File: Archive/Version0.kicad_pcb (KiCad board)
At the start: 2 copper layers, 14 parts, among them P1 CONN_BATT, P2 CONN_LOAD, P3 CONN_VREG, P4 CONN_FEATHER12, P5 CONN_FEATHER16, P6 CONN_RB, P7 CONN_WS, P8 CONN_RB, P9 CONN_WS, Q1 Q_NMOS_GDS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

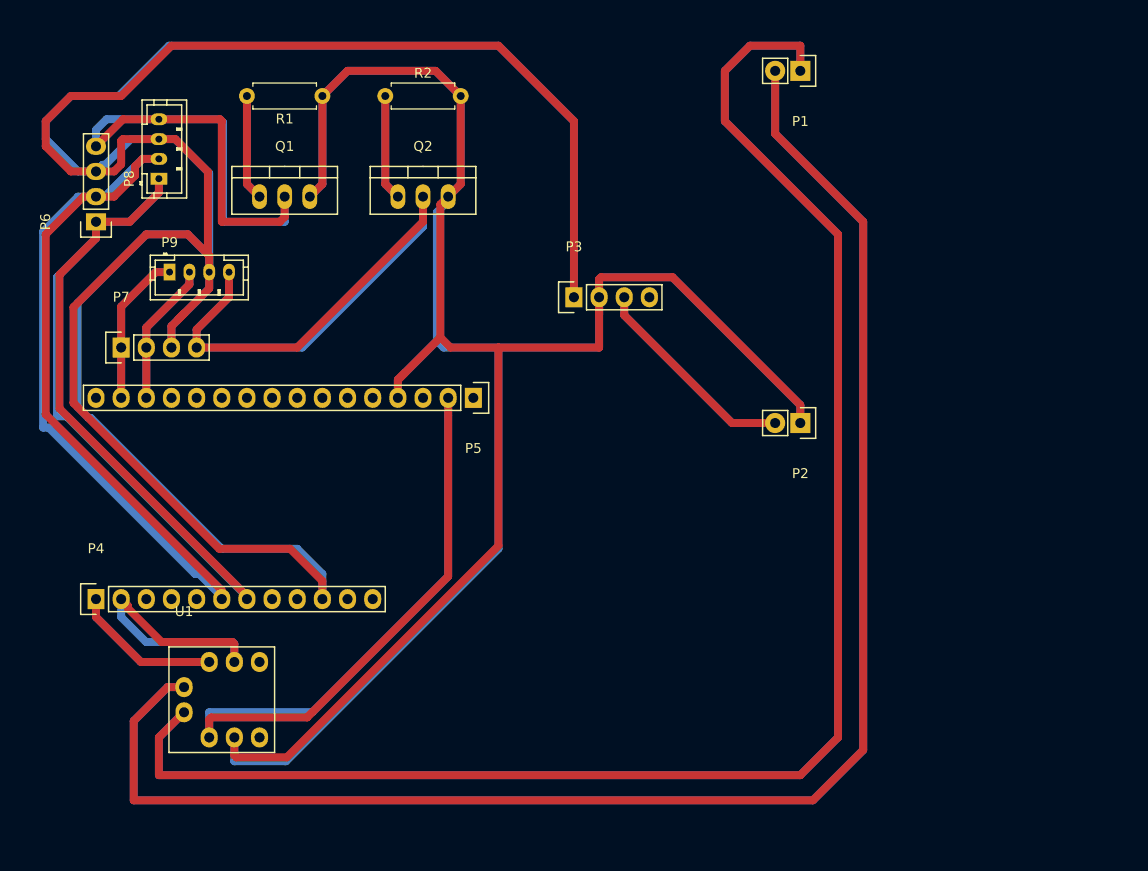
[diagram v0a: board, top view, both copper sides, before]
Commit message: Fixed Gerbers
Updated the footprint pins on the Fuel Gauge
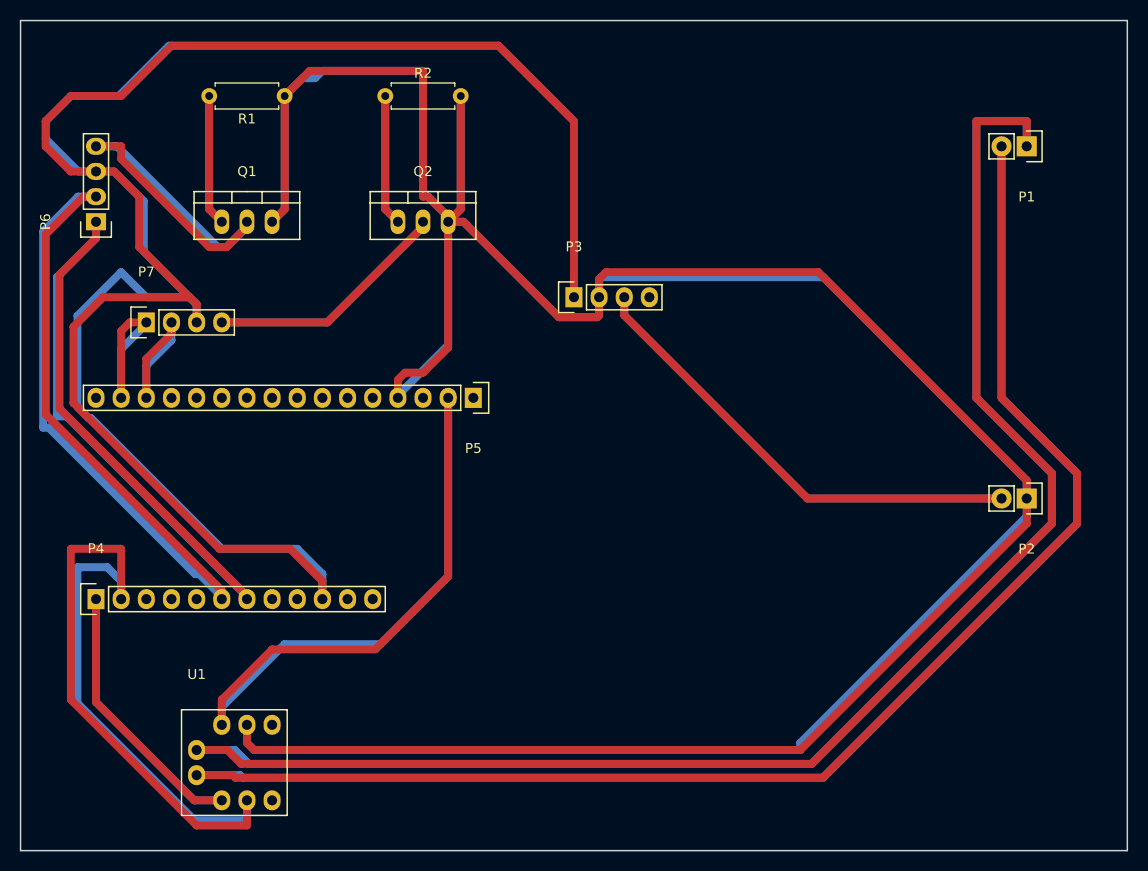
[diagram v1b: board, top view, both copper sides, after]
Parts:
- removed P8: CONN_RB, Connectors_JST:JST_PH_B4B-PH-K_04x2.00mm_Straight
- removed P9: CONN_WS, Connectors_JST:JST_PH_B4B-PH-K_04x2.00mm_Straight
- moved P1 24.1 mm to (177.8, 38.1)
- moved P2 24.1 mm to (177.8, 73.7)
- moved U1 6.48 mm to (94.0, 96.5)
- moved Q1 4.58 mm to (99.1, 45.7)
- moved R1 3.81 mm to (102.9, 33.0)
- moved P7 3.59 mm to (88.9, 55.9)
- moved Q2 2.54 mm to (116.8, 45.7)
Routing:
- net GND: track 342.9 -> 496.4 mm
- net /SCL: track 31.5 -> 95.4 mm
- net /VLOAD: track 43.1 -> 95.2 mm
- net /B+: track 325.1 -> 281.8 mm
- net +5V: track 367.8 -> 328.6 mm
- net Net-(P7-Pad4): track 79.6 -> 49.6 mm
- net Net-(P6-Pad4): track 66.5 -> 42.3 mm
- net /SDA: track 30.2 -> 54.4 mm
- net (no net): track 22.9 -> 0.00 mm
- net /B-: track 321.6 -> 298.8 mm
- net /RBRX: track 113.7 -> 95.7 mm
- net /RBTX: track 119.2 -> 102.8 mm
- net /WSRX: track 31.1 -> 18.3 mm
- net /WSTX: track 29.0 -> 17.3 mm
- net Net-(Q2-Pad1): track 21.4 -> 26.5 mm
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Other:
- board outline added: 111.8 x 83.8 mm
